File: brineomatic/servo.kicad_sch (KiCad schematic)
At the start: 1 part

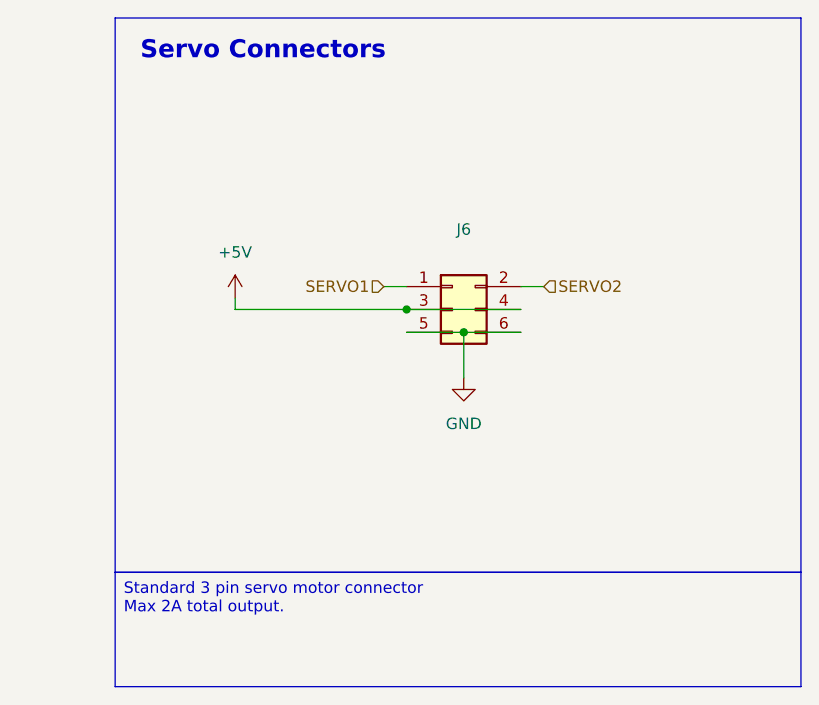
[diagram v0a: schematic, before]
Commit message: 5v power supply is sorted.
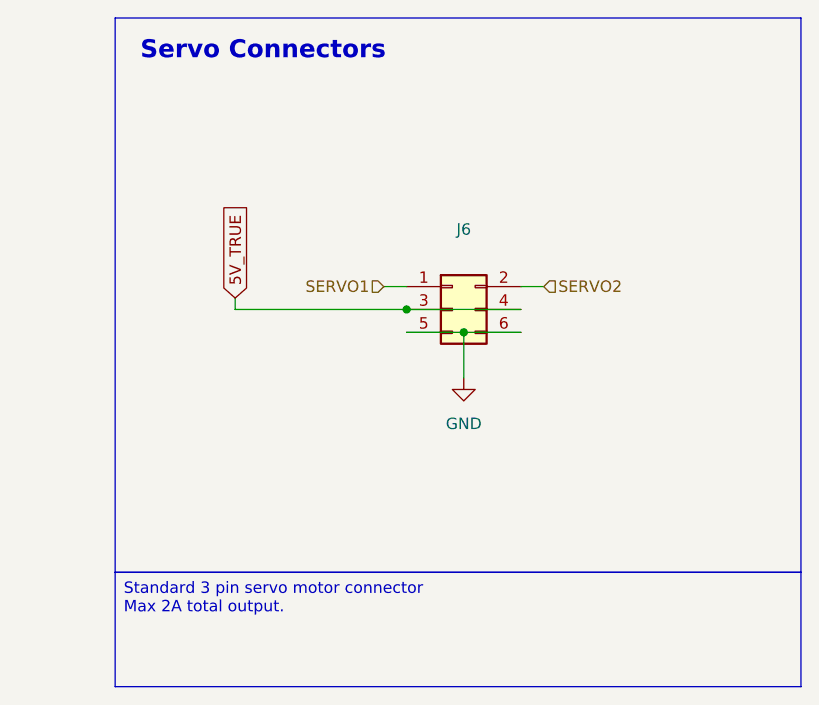
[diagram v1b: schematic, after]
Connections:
- net +5V renamed 5V_TRUE
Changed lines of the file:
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@@
+		)
+	)
+	(global_label "5V_TRUE"
+		(shape input)
+		(at 111.76 95.25 90)
+		(fields_autoplaced yes)
+		(effects
+			(font
+				(size 1.27 1.27)
+			)
+			(justify left)
+		)
+		(property "Intersheetrefs" "${INTERSHEET_REFS}"
+			(at 111.76 84.282 90)
+			(effects
+				(font
+					(size 1.27 1.27)
+				)
+				(justify left)
+				(hide yes)
+			)
 		)
 	)
@@
 		)
 	)
-	(symbol
-		(lib_id "power:+5V")
-		(at 111.76 95.25 0)
-		(unit 1)
-		(exclude_from_sim no)
-		(in_bom yes)
-		(on_board yes)
-		(dnp no)
-		(fields_autoplaced yes)
-		(property "Reference" "#PWR019"
-			(at 111.76 99.06 0)
-			(effects
-				(font
-					(size 1.27 1.27)
-				)
-				(hide yes)
-			)
-		)
-		(property "Value" "+5V"
-			(at 111.76 90.17 0)
-			(effects
-				(font
-					(size 1.27 1.27)
-				)
-			)
-		)
-		(property "Footprint" ""
-			(at 111.76 95.25 0)
-			(effects
-				(font
-					(size 1.27 1.27)
-				)
-				(hide yes)
-			)
-		)
-		(property "Datasheet" ""
-			(at 111.76 95.25 0)
-			(effects
-				(font
-					(size 1.27 1.27)
-				)
-				(hide yes)
-			)
-		)
-		(property "Description" "Power symbol creates a global label with name \"+5V\""
-			(at 111.76 95.25 0)
-			(effects
-				(font
-					(size 1.27 1.27)
-				)
-				(hide yes)
-			)
-		)
-		(pin "1"
-		)
-		(instances
-			(project ""
-				(path "/96477ae2-ef08-48f3-8dd4-fe4478541f68/0442c100-f200-44e3-9806-ad19ad5a87d8"
-					(reference "#PWR019")
-					(unit 1)
-				)
-			)
-		)
-	)

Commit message: all connectors are now flush withe 3mm outside edge of the case
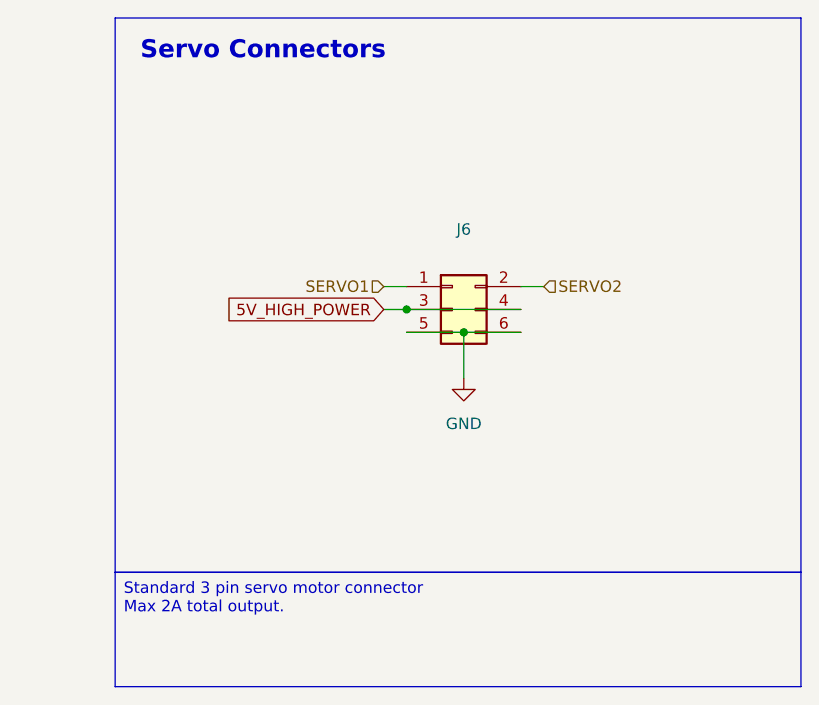
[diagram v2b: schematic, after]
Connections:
- net 5V_TRUE renamed 5V_HIGH_POWER
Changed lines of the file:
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@@
 	(wire
 		(pts
-			(xy 130.81 96.52) (xy 111.76 96.52)
+			(xy 130.81 96.52) (xy 128.27 96.52)
 		)
 		(stroke
@@
 		)
 	)
-	(wire
-		(pts
-			(xy 111.76 96.52) (xy 111.76 95.25)
-		)
-		(stroke
-			(width 0)
-			(type default)
-		)
-	)
-	(global_label "5V_TRUE"
+	(global_label "5V_HIGH_POWER"
 		(shape input)
-		(at 111.76 95.25 90)
+		(at 128.27 96.52 180)
 		(fields_autoplaced yes)
 		(effects
@@
 				(size 1.27 1.27)
 			)
-			(justify left)
+			(justify right)
 		)
 		(property "Intersheetrefs" "${INTERSHEET_REFS}"
-			(at 111.76 84.282 90)
+			(at 110.0448 96.52 0)
 			(effects
 				(font
 					(size 1.27 1.27)
 				)
-				(justify left)
+				(justify right)
 				(hide yes)
 			)

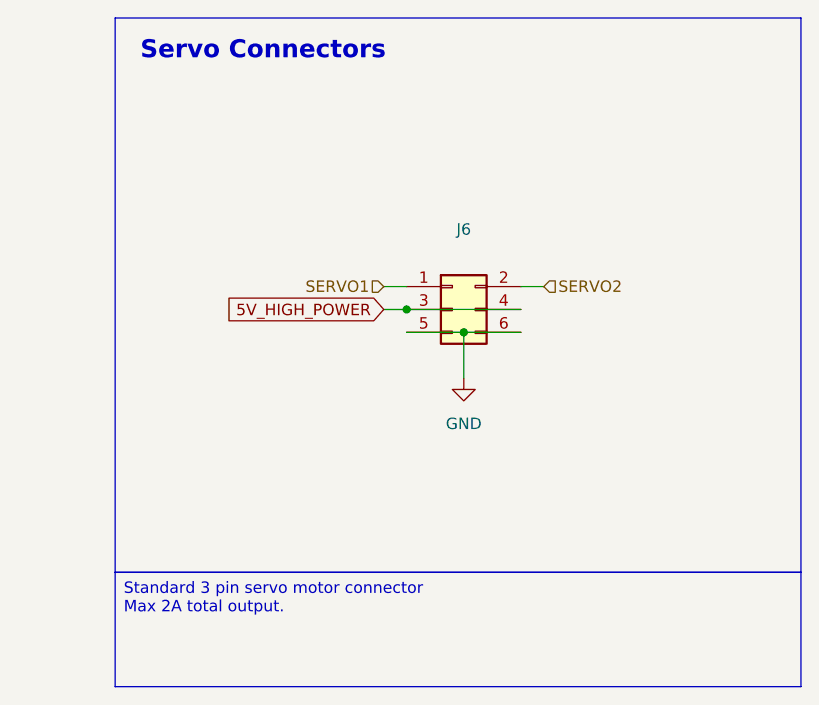
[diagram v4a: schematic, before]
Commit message: more esd protection, drc passing, silkscreen fixed
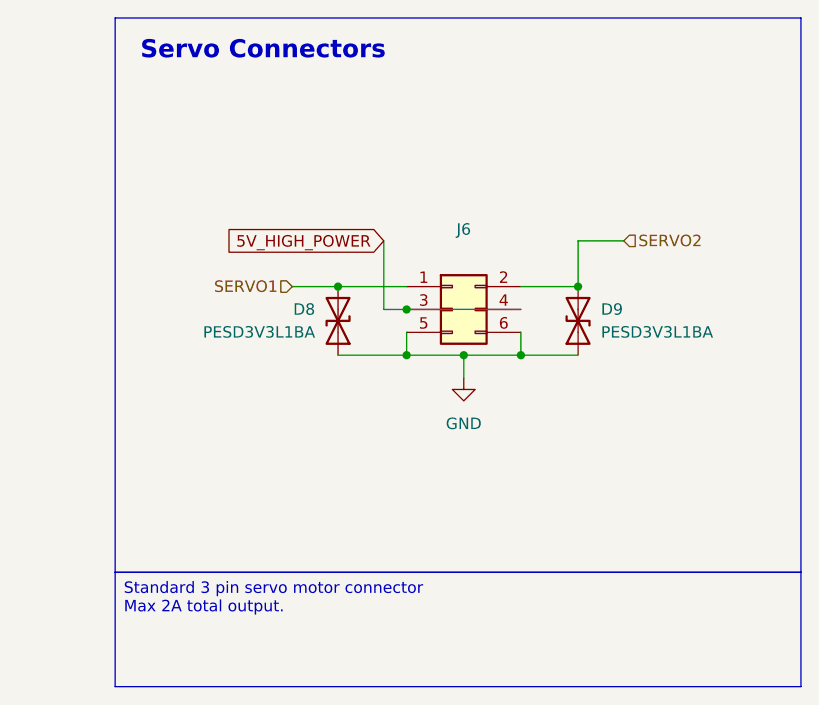
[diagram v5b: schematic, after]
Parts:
- added D8, D9: PESD3V3L1BA, Diode_SMD:D_SOD-323, symbol Device:D_TVS
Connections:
- net GND: now also D8.1 (A1), D9.1 (A1)
- net SERVO1: now also D8.2 (A2)
- net SERVO2: now also D9.2 (A2)

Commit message: added more esd protection to the power rails (24v, 5v, 3.3v)
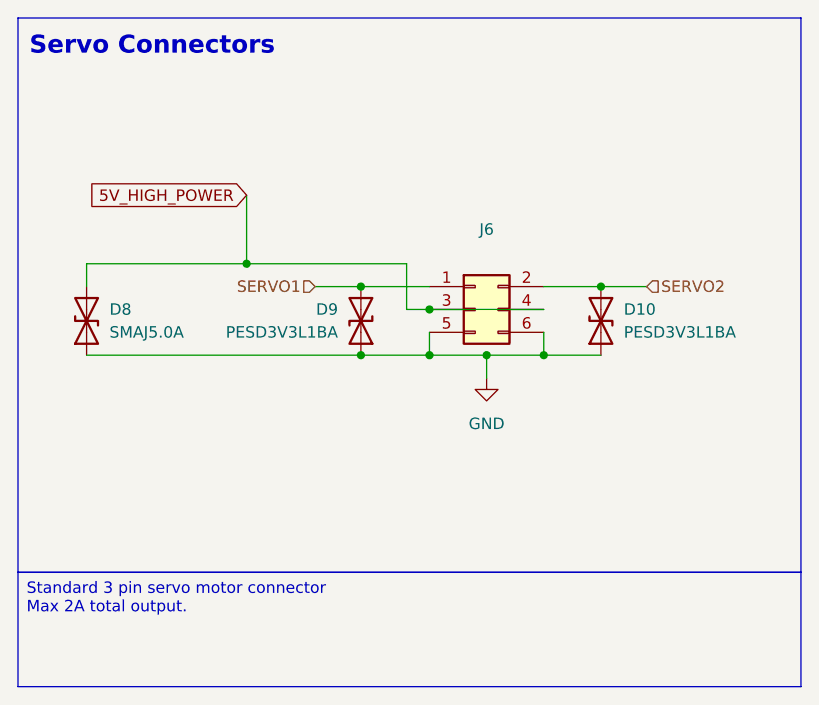
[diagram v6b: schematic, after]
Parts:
- added D8: SMAJ5.0A, Diode_SMD:D_SMA, symbol Device:D_TVS
- D10: renamed from D9; LCSC (none) -> C2687129
- D9: renamed from D8; LCSC (none) -> C2687129
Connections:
- net 5V_HIGH_POWER: now also D8.2 (A2)
- net GND: now also D8.1 (A1)
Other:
- moved on the sheet: D10, D9, J6

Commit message: add inline resistor to temperature sensor + servo inputs - 100ohm
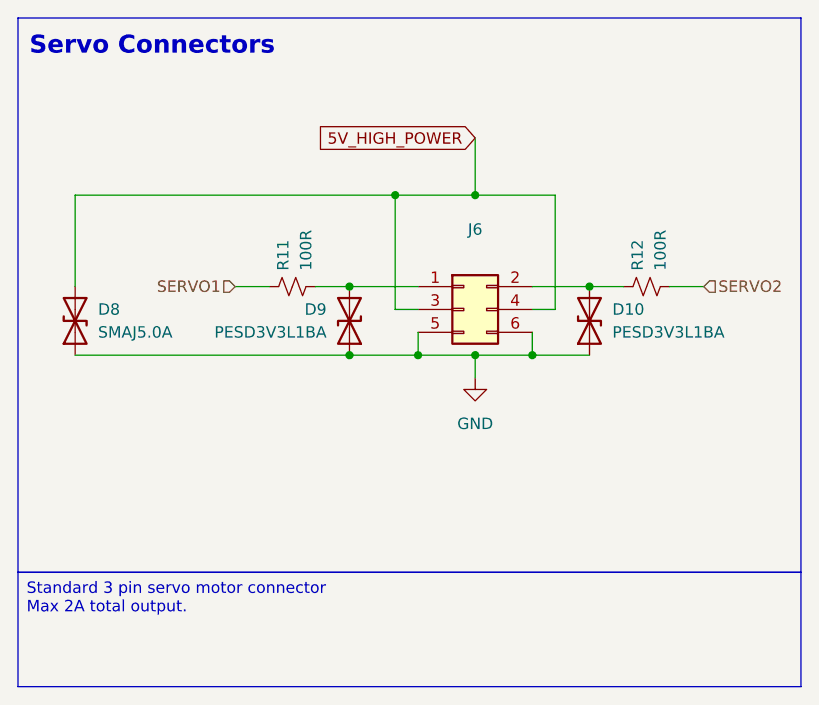
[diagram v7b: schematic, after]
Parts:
- added R11, R12: 100R, Resistor_SMD:R_0603_1608Metric, symbol Device:R_Small_US
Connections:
- net SERVO1: now also R11.2; no longer D9.2 (A2), J6.1 (Pin_1)
- net SERVO2: now also R12.1; no longer D10.2 (A2), J6.2 (Pin_2)
- new net: D10.2 (A2), J6.2 (Pin_2), R12.2
- new net: D9.2 (A2), J6.1 (Pin_1), R11.1
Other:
- moved on the sheet: D10, D8, D9, J6

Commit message: updated analog sensor esd schematic
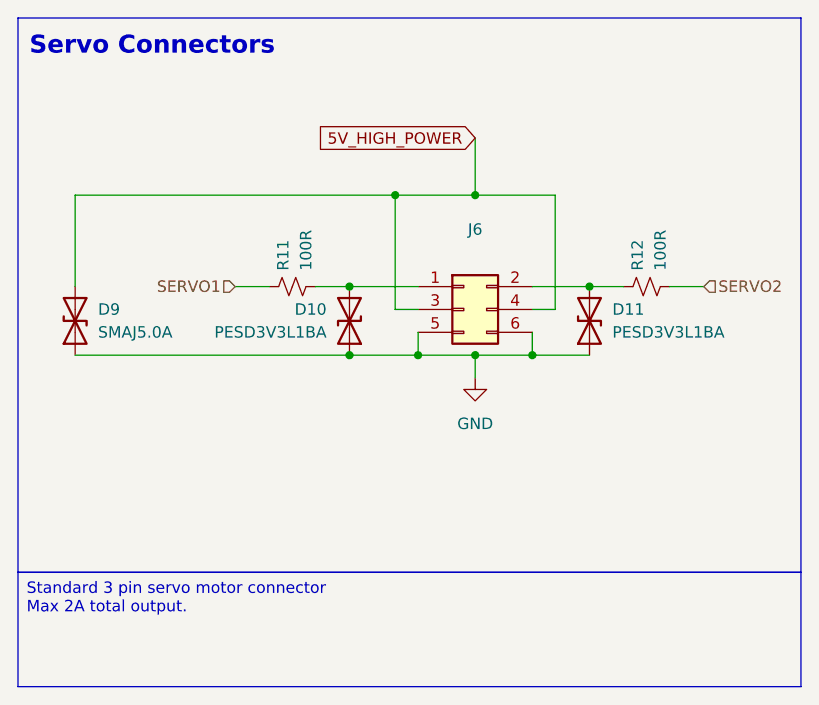
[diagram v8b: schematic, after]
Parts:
- renumbered D9 to D10, D10 to D11, D8 to D9
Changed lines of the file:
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@@
 		(on_board yes)
 		(dnp no)
-		(property "Reference" "D9"
+		(property "Reference" "D10"
 			(at 121.92 96.5199 90)
 			(effects
@@
 			(project "brineomatic"
 				(path "/96477ae2-ef08-48f3-8dd4-fe4478541f68/0442c100-f200-44e3-9806-ad19ad5a87d8"
-					(reference "D9")
+					(reference "D10")
 					(unit 1)
 				)
@@
 		(on_board yes)
 		(dnp no)
-		(property "Reference" "D8"
+		(property "Reference" "D9"
 			(at 96.52 96.52 90)
 			(effects
@@
 			(project "brineomatic"
 				(path "/96477ae2-ef08-48f3-8dd4-fe4478541f68/0442c100-f200-44e3-9806-ad19ad5a87d8"
-					(reference "D8")
+					(reference "D9")
 					(unit 1)
 				)
@@
 		(dnp no)
 		(fields_autoplaced yes)
-		(property "Reference" "D10"
+		(property "Reference" "D11"
 			(at 153.67 96.5199 90)
 			(effects
@@
 			(project "brineomatic"
 				(path "/96477ae2-ef08-48f3-8dd4-fe4478541f68/0442c100-f200-44e3-9806-ad19ad5a87d8"
-					(reference "D10")
+					(reference "D11")
 					(unit 1)
 				)
@@
 		(dnp no)
 		(fields_autoplaced yes)
-		(property "Reference" "#PWR019"
+		(property "Reference" "#PWR020"
 			(at 138.43 110.49 0)
 			(effects
@@
 			(project "brineomatic"
 				(path "/96477ae2-ef08-48f3-8dd4-fe4478541f68/0442c100-f200-44e3-9806-ad19ad5a87d8"
-					(reference "#PWR019")
+					(reference "#PWR020")
 					(unit 1)
 				)
